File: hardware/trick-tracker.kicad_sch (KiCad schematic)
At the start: 50 parts, among them IC1 BMX160, J1 USB4105-GF-A, J2 S2B-PH-K, J3 QWiiC, J4 MEM2061-01-188-00-A, J6 QWiiC, P1 SMTB-1240-S-R, U2 DPS368XTSA1, U3 ESP32-WROOM-32, U4 MCP73831/OT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

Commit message: current changed (to be checked again)
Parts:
- removed D1, D5: DSS13UTR, Diode_SMD:D_SOD-123F, symbol Device:D_Schottky
- removed J4: MEM2061-01-188-00-A, MEM2051-00-195-00-A:GCT_MEM2051-00-195-00-A, symbol MEM2051-00-195-00-A:MEM2051-00-195-00-A
- removed R8: 10k, Resistor_SMD:R_0603_1608Metric, symbol Device:R_Small
- added C?: 10µF, Capacitor_SMD:C_0603_1608Metric, symbol Device:C_Small
- added J4: MEM2061-01-188-00-A_REVA, MEM2061-01-188-00-A_REVA:GCT_MEM2061-01-188-00-A_REVA, symbol MEM2061-01-188-00-A_REVA:MEM2061-01-188-00-A_REVA
- added R?: 10k, Resistor_SMD:R_0603_1608Metric, symbol Device:R_Small
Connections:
- net VIN is gone; now on net VBAT: C1.1, S3.3 (COM), U5.1 (VIN)
- net +3V3: now also J4.4 (VDD), R?.2
- net BTN: now also C11.1, R15.1, S1.1 (NO), S1.3 (NO); no longer C7.1, S2.1 (NO), S2.3 (NO)
- net CLK: now also J4.5 (CLK)
- net CS: now also J4.2 (CD/DAT3)
- net GND: now also C?.2, J4.11 (GND), J4.12 (GND), J4.6 (VSS)
- net MISO: now also J4.7 (DAT0)
- net MOSI: now also J4.3 (CMD)
- net SD_DETECT: now also J4.10 (CD2), J4.9 (CD1)
- net BOOT: now reaches U3.25 (IO0)
- net BOOT: now also C7.1, S2.1 (NO), S2.3 (NO)
- removed net RESET: C11.1, R15.1, S1.1 (NO), S1.3 (NO), U3.3 (EN)
- new net ESP_EN: C?.1, R?.1, U3.3 (EN)
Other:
- moved on the sheet: C11, C7, R15, R16, R17, S1, S2

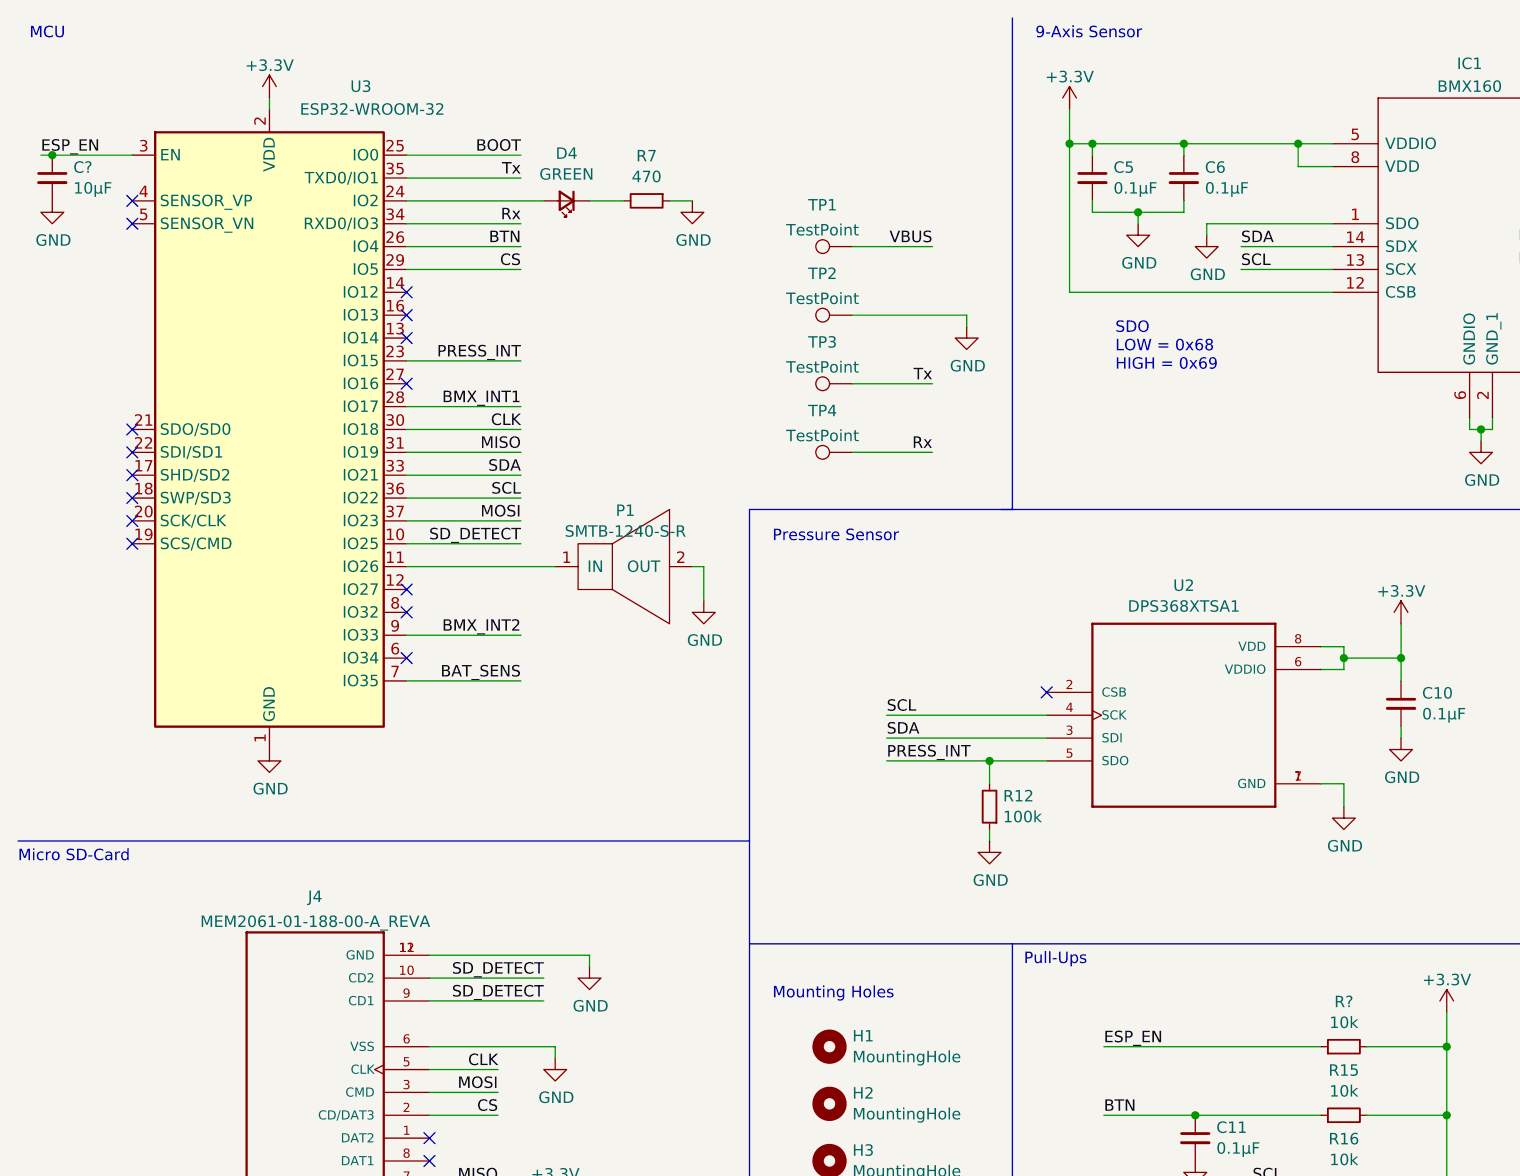
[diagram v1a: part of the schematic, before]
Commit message: add testpoints + test programms
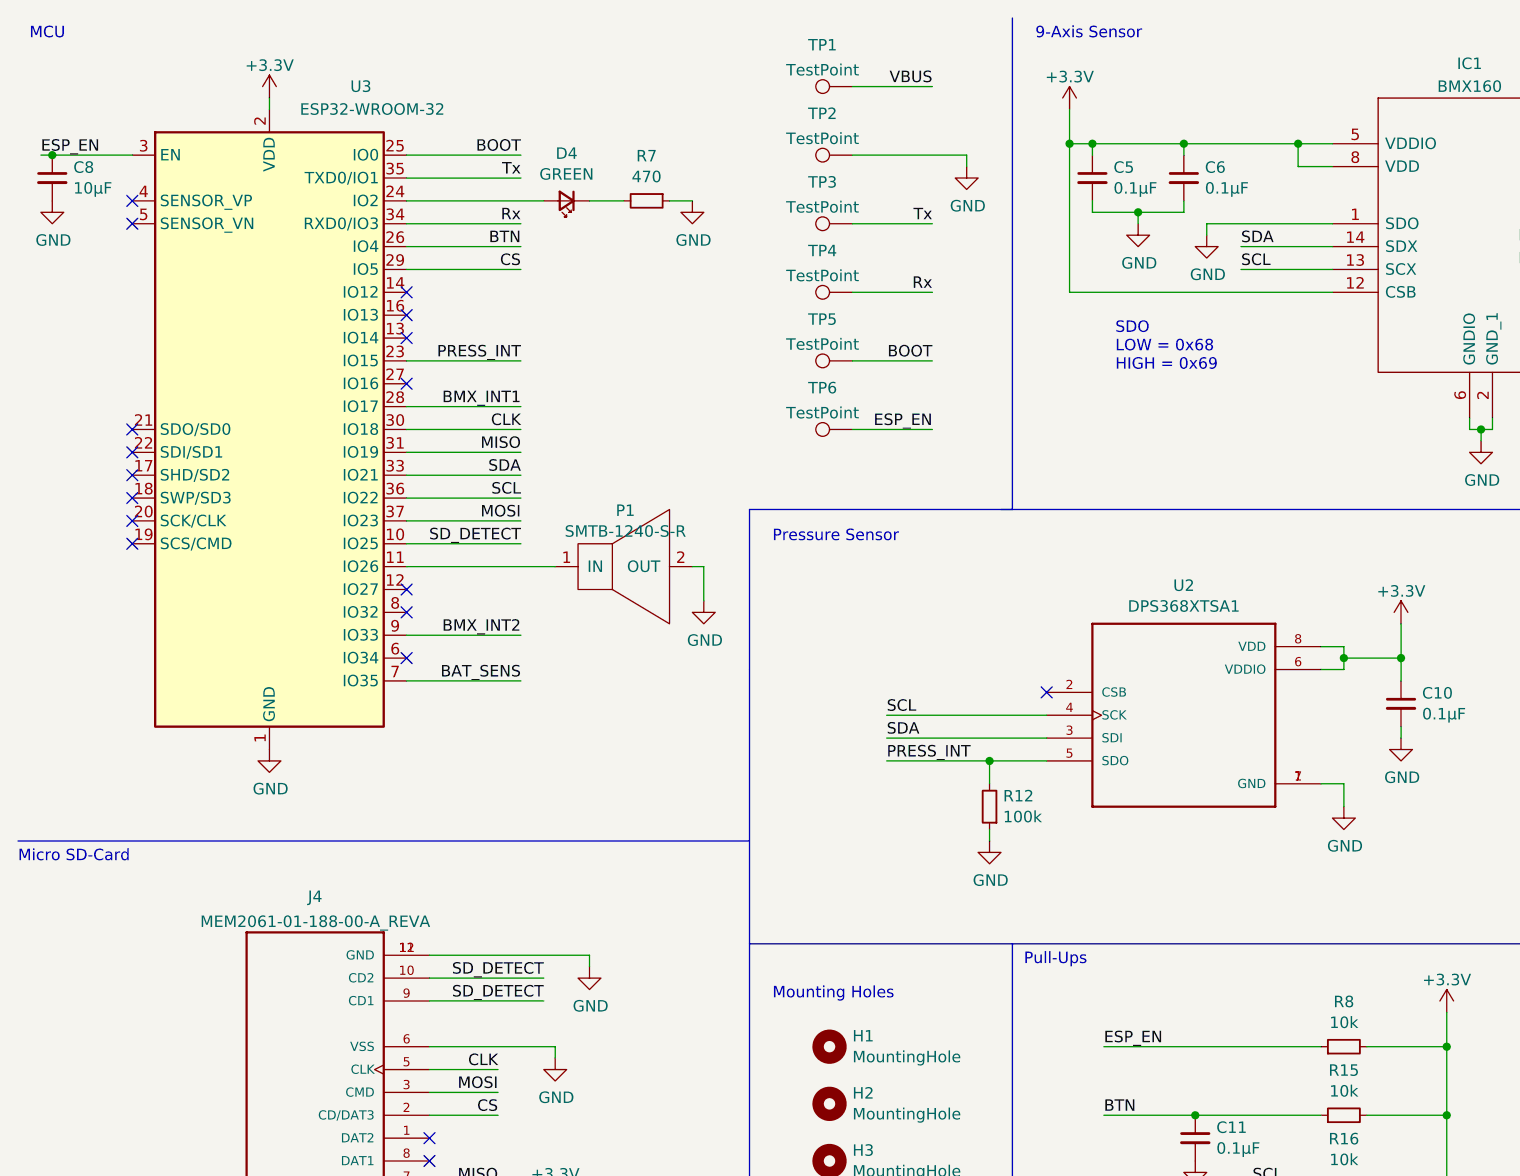
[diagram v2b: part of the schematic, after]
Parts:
- added TP5, TP6: TestPoint, TestPoint:TestPoint_Pad_D1.5mm, symbol Connector:TestPoint
- gave numbers to parts that had none: 2
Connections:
- net BOOT: now also TP5.1
- net ESP_EN: now also TP6.1
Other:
- moved on the sheet: TP1, TP2, TP3, TP4

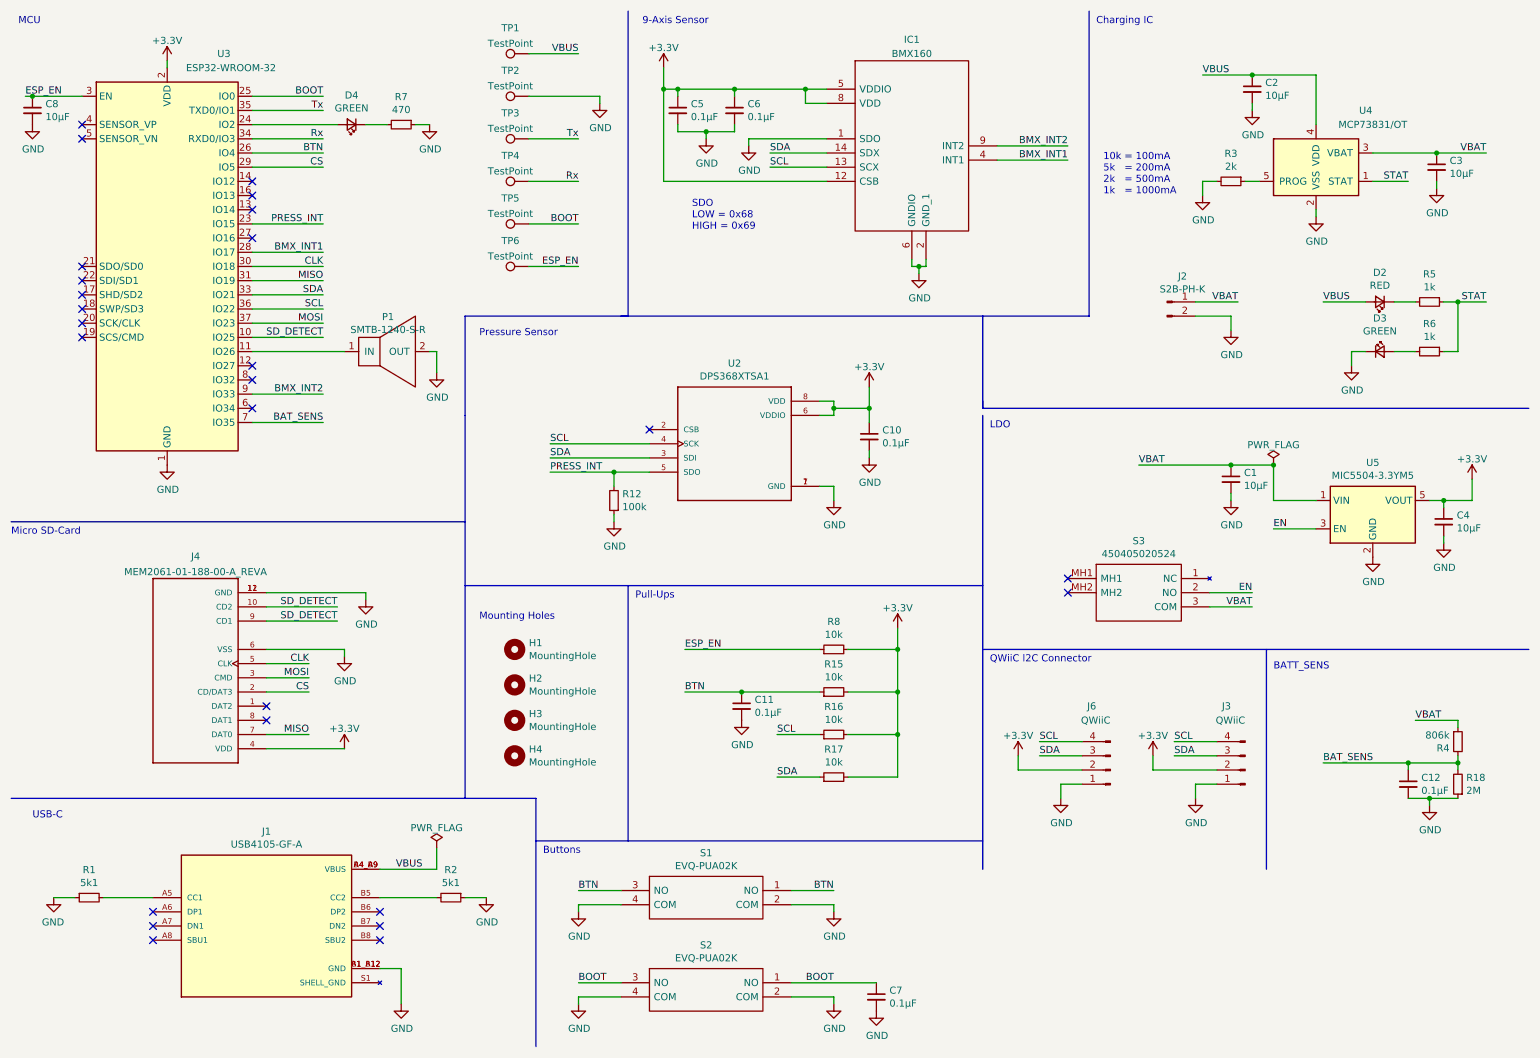
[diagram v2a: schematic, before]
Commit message: Changed schematics and layout to fit current changes
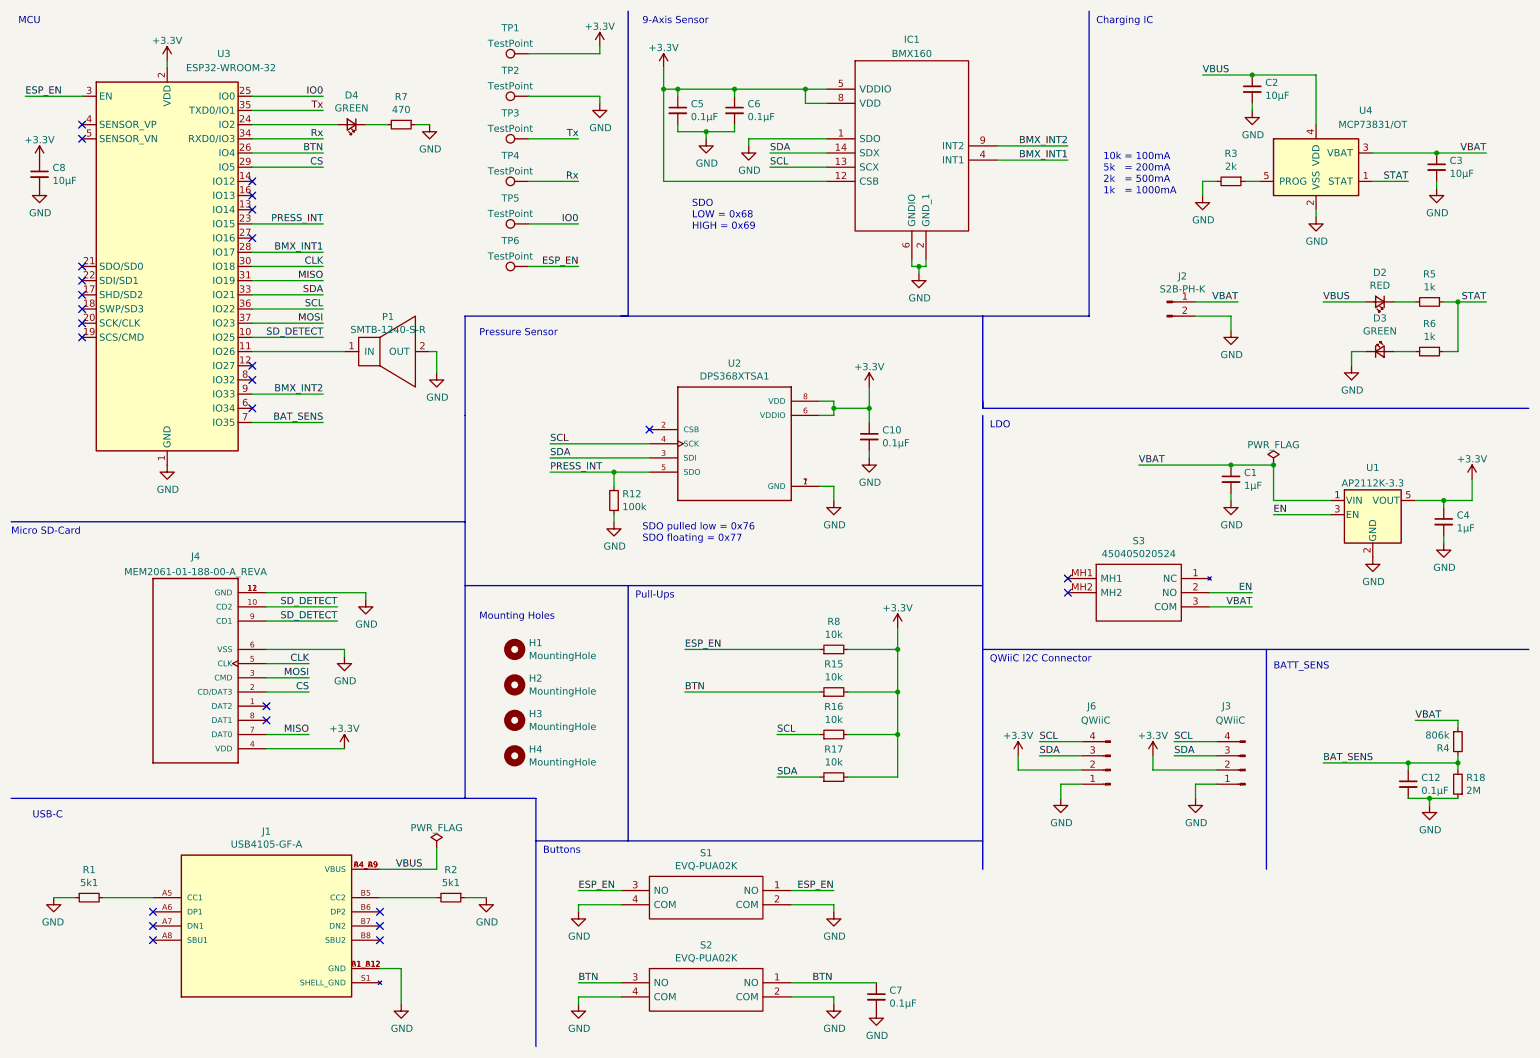
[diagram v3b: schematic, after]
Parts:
- removed C11: 0.1µF, Capacitor_SMD:C_0603_1608Metric, symbol Device:C_Small
- removed U5: MIC5504-3.3YM5, Package_TO_SOT_SMD:SOT-23-5, symbol Regulator_Linear:MIC5504-3.3YM5
- added U1: AP2112K-3.3, Package_TO_SOT_SMD:SOT-23-5, symbol Regulator_Linear:AP2112K-3.3
- C1, C4: value 10µF -> 1µF
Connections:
- net +3V3: now also C8.1, TP1.1, U1.5 (VOUT)
- net BTN: now also C7.1, S2.1 (NO), S2.3 (NO); no longer S1.1 (NO), S1.3 (NO)
- net EN: now also U1.3 (EN)
- net ESP_EN: now also S1.1 (NO), S1.3 (NO); no longer C8.1
- net GND: now also U1.2 (GND)
- net VBAT: now also U1.1 (VIN)
- net VBUS: no longer TP1.1
- removed net BOOT: C7.1, S2.1 (NO), S2.3 (NO), TP5.1, U3.25 (IO0)
- new net IO0: TP5.1, U3.25 (IO0)
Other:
- note added: "SDO pulled low = 0x76 SDO floating = 0x77"
- moved on the sheet: C8
